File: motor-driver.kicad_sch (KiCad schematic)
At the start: 0 parts

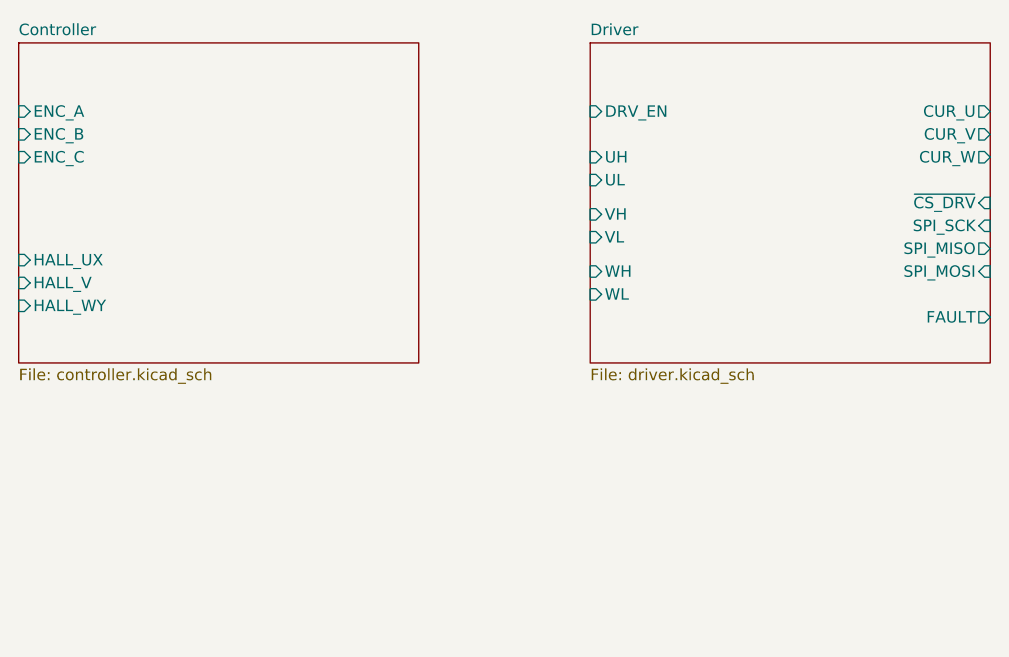
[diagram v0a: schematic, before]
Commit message: Finish controller and driver schematics.
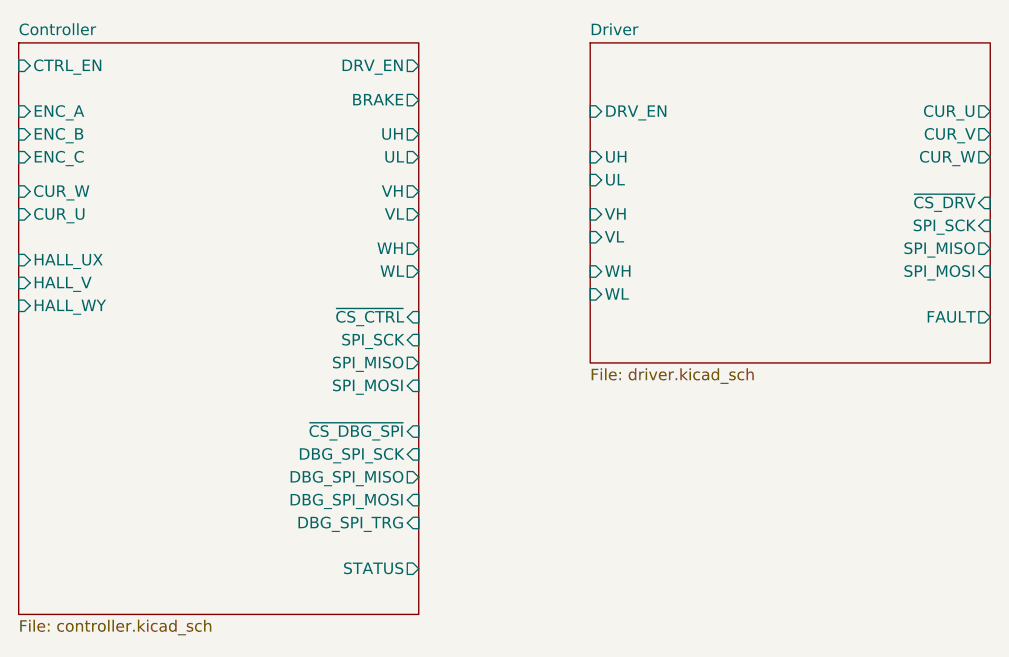
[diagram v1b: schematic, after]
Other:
- sheet Controller ports: added BRAKE, CTRL_EN, CUR_U, CUR_W, DBG_SPI_MISO, DBG_SPI_MOSI, DBG_SPI_SCK, DBG_SPI_TRG, DRV_EN, SPI_MISO, SPI_MOSI, SPI_SCK, STATUS, UH, UL, VH, VL, WH, WL, ~{CS_CTRL}, ~{CS_DBG_SPI}; removed none
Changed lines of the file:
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@@
 (kicad_sch (version 20230121) (generator eeschema)
   (paper "A4")
-  (sheet (at 116.84 68.58) (size 44.45 35.56) (fields_autoplaced)
+  (sheet (at 116.84 68.58) (size 44.45 63.5) (fields_autoplaced)
     (stroke (width 0.1524) (type solid))
     (fill (color 0 0 0 0.0000))
@@
       (effects (font (size 1.27 1.27)) (justify left bottom))
     )
-    (property "Sheetfile" "controller.kicad_sch" (at 116.84 104.7246 0)
+    (property "Sheetfile" "controller.kicad_sch" (at 116.84 132.6646 0)
       (effects (font (size 1.27 1.27)) (justify left top))
     )
@@
       (effects (font (size 1.27 1.27)) (justify left))
     )
+    (pin "CTRL_EN" input (at 116.84 71.12 180)
+      (effects (font (size 1.27 1.27)) (justify left))
+    )
+    (pin "~{CS_CTRL}" input (at 161.29 99.06 0)
+      (effects (font (size 1.27 1.27)) (justify right))
+    )
+    (pin "SPI_SCK" input (at 161.29 101.6 0)
+      (effects (font (size 1.27 1.27)) (justify right))
+    )
+    (pin "SPI_MOSI" input (at 161.29 106.68 0)
+      (effects (font (size 1.27 1.27)) (justify right))
+    )
+    (pin "SPI_MISO" output (at 161.29 104.14 0)
+      (effects (font (size 1.27 1.27)) (justify right))
+    )
+    (pin "~{CS_DBG_SPI}" input (at 161.29 111.76 0)
+      (effects (font (size 1.27 1.27)) (justify right))
+    )
+    (pin "DBG_SPI_MOSI" input (at 161.29 119.38 0)
+      (effects (font (size 1.27 1.27)) (justify right))
+    )
+    (pin "DBG_SPI_SCK" input (at 161.29 114.3 0)
+      (effects (font (size 1.27 1.27)) (justify right))
+    )
+    (pin "DBG_SPI_MISO" output (at 161.29 116.84 0)
+      (effects (font (size 1.27 1.27)) (justify right))
+    )
+    (pin "DBG_SPI_TRG" input (at 161.29 121.92 0)
+      (effects (font (size 1.27 1.27)) (justify right))
+    )
+    (pin "CUR_W" input (at 116.84 85.09 180)
+      (effects (font (size 1.27 1.27)) (justify left))
+    )
+    (pin "CUR_U" input (at 116.84 87.63 180)
+      (effects (font (size 1.27 1.27)) (justify left))
+    )
+    (pin "UH" output (at 161.29 78.74 0)
+      (effects (font (size 1.27 1.27)) (justify right))
+    )
+    (pin "UL" output (at 161.29 81.28 0)
+      (effects (font (size 1.27 1.27)) (justify right))
+    )
+    (pin "VH" output (at 161.29 85.09 0)
+      (effects (font (size 1.27 1.27)) (justify right))
+    )
+    (pin "BRAKE" output (at 161.29 74.93 0)
+      (effects (font (size 1.27 1.27)) (justify right))
+    )
+    (pin "STATUS" output (at 161.29 127 0)
+      (effects (font (size 1.27 1.27)) (justify right))
+    )
+    (pin "DRV_EN" output (at 161.29 71.12 0)
+      (effects (font (size 1.27 1.27)) (justify right))
+    )
+    (pin "WH" output (at 161.29 91.44 0)
+      (effects (font (size 1.27 1.27)) (justify right))
+    )
+    (pin "VL" output (at 161.29 87.63 0)
+      (effects (font (size 1.27 1.27)) (justify right))
+    )
+    (pin "WL" output (at 161.29 93.98 0)
+      (effects (font (size 1.27 1.27)) (justify right))
+    )
     (instances
